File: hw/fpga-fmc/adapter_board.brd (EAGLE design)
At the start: 69 x 84 mm, 167 parts, among them IC1 M24C02, J1 5569262-1, J2 ASP-134488-01, U1 ADM3066E, U10 ADM3066E, U11 ADM3066E, U12 ADM3066E, U13 ADM3066E, U14 ADM3066E, U15 ADM3066E, U16 ADM3066E, U17 TCA9548A, U18 TXS0102, U19 TXS0102, U2 ADM3066E, U20 TXS0102, U21 TXS0102, U3 ADM3066E, U4 ADM3066E, U5 ADM3066E, U6 ADM3066E, U7 ADM3066E, U8 ADM3066E, U9 ADM3066E

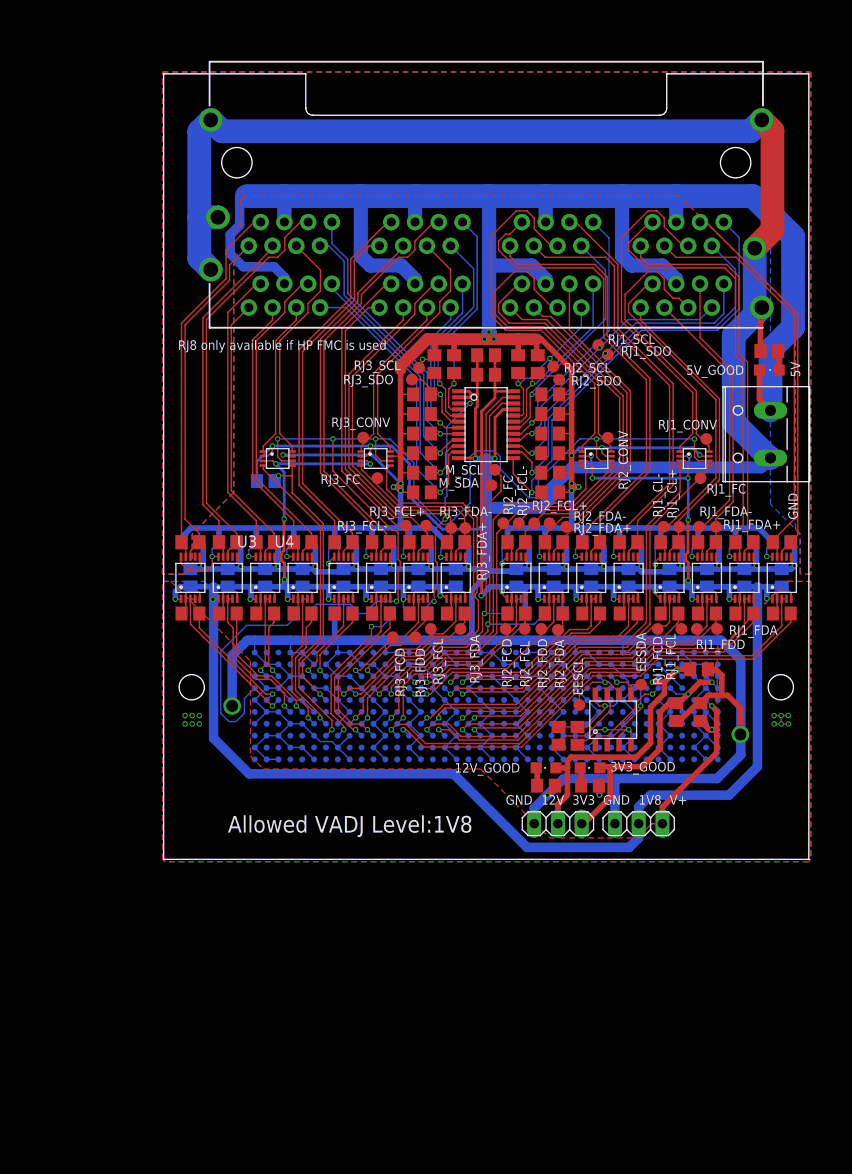
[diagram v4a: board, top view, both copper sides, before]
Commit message: hw/fpga-fmc: fix connector turned by 180 degrees. add led for 1v8. change i2c package
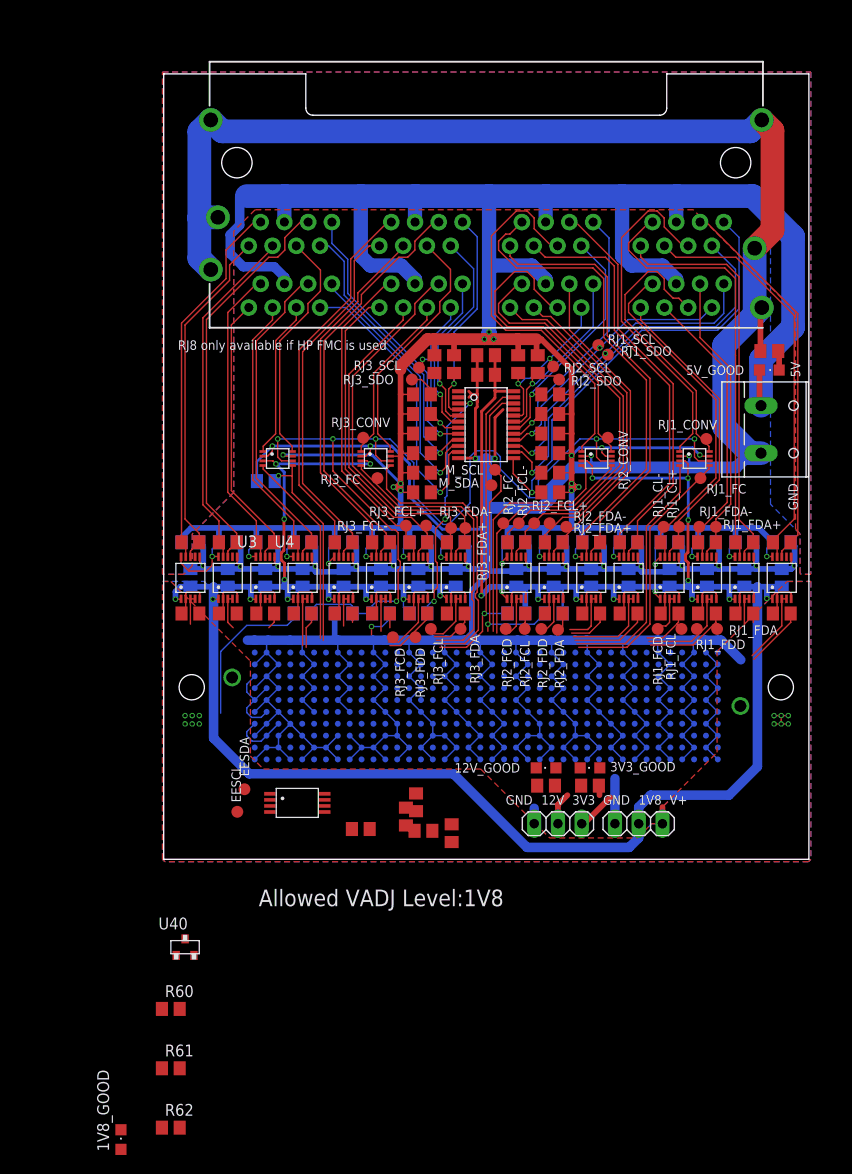
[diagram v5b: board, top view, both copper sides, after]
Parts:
- added 1V8_GOOD: (no value), led:CHIPLED_0805
- added R60: 10R, resistor:R0805
- added R61: 10k, resistor:R0805
- added R62: 130R, resistor:R0805
- added U40: IRLML2502, parts:SOT23-IRLML
- IC1: device parts:SO8N -> parts:TSSOP-8
- moved EESDA 43.9 mm to (8.64, 7.49)
- moved EESCL 38.3 mm to (7.87, 5.08)
- moved C36 36.0 mm to (21.1, 3.24), turned to 180 degrees
- moved IC1 34.9 mm to (14.3, 6.03)
- moved C37 34.2 mm to (27.8, 3.05)
- moved C35 33.4 mm to (25.9, 4.57)
- moved C39 17.0 mm to (30.8, 2.79)
- moved R52 16.8 mm to (27.0, 6.10)
- moved X1 0.57 mm to (64.5, 46.0), turned to 270 degrees
- turned J2 to 180 degrees
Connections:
- new net N$6: R60.1, R61.1, U40.P1
- new net N$8: R62.2, U40.P3
- new net N$9: 1V8_GOOD.C, R62.1
- net +3V3: now also 1V8_GOOD.A
- net 0V: now also IC1.3, IC1.4, R61.2, U40.P2, X1.2; no longer IC1.P3, IC1.P4, U17.P0, U17.P1, X1.1
- net 1V8: now also R60.2
- net 3P3VAUX: now also IC1.8; no longer IC1.P8
- net 5V: now also X1.1; no longer X1.2
- net FMC_IIC_SCL: now also IC1.6, M_SCL.TP, R6.1, U17.P21; no longer IC1.P6
- net FMC_IIC_SDA: now also IC1.5, M_SDA.TP, R5.1, U17.P22; no longer IC1.P5
- net FMC_LA05_N: no longer M_SCL.TP, R6.1, U17.P21
- net FMC_LA05_P: no longer M_SDA.TP, R5.1, U17.P22
- net GA0: now also IC1.2, U17.P1; no longer IC1.P2
- net GA1: now also IC1.1, U17.P0; no longer IC1.P1
- net N$1: now also IC1.7; no longer IC1.P7
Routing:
- net 0V: track 783.7 -> 718.4 mm, vias 38 -> 34
- net FMC_LA05_N: track 48.2 -> 0.00 mm, vias 2 -> 0
- net FMC_LA05_P: track 44.8 -> 0.00 mm, vias 2 -> 0
- net FMC_LA07_P: track 52.3 -> 7.88 mm, vias 1 -> 0
- net FMC_LA07_N: track 49.6 -> 6.52 mm, vias 1 -> 0
- net FMC_LA11_P: track 43.9 -> 3.39 mm, vias 1 -> 0
- net FMC_LA11_N: track 41.1 -> 0.95 mm, vias 1 -> 0
- net FMC_IIC_SDA: track 4.60 -> 35.4 mm
- net +12V: track 31.6 -> 3.47 mm, vias 2 -> 0
- net FMC_IIC_SCL: track 7.74 -> 33.8 mm
- net FMC_LA16_P: track 30.7 -> 5.25 mm, vias 1 -> 0
- net FMC_LA15_P: track 35.6 -> 10.9 mm, vias 1 -> 0
- net FMC_LA15_N: track 33.0 -> 9.52 mm, vias 1 -> 0
- net FMC_LA16_N: track 28.6 -> 5.72 mm, vias 1 -> 0
- net FMC_LA12_P: track 46.9 -> 26.6 mm, vias 1 -> 0
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
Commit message: hdl: copy all pin assignments to constraint file
note: RJ8 FMC connection are not connected on the FPGA board, so RJ8 cannot be used with the prototype pcb
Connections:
- net FMC_HA00_CC_N: no longer J2.F5
- net FMC_HA00_CC_P: no longer J2.F4
- net FMC_HA01_CC_N: no longer J2.E3
- net FMC_HA01_CC_P: no longer J2.E2
- net FMC_HA05_N: no longer J2.E7
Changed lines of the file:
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@@
 </signal>
 <signal name="FMC_HA01_CC_P">
-<contactref element="J2" pad="E2"/>
 <contactref element="R2" pad="2"/>
 <wire x1="3.8075" y1="26.289" x2="4.318" y2="26.289" width="0.1524" layer="1"/>
-<wire x1="4.318" y1="26.289" x2="57.995" y2="15.765" width="0" layer="19" extent="1-16"/>
 </signal>
 <signal name="FMC_HA01_CC_N">
-<contactref element="J2" pad="E3"/>
 <contactref element="U1" pad="P2"/>
 <contactref element="U1" pad="P3"/>
 <wire x1="2.8575" y1="27.849" x2="3.3575" y2="27.849" width="0.1524" layer="1"/>
 <wire x1="2.8575" y1="27.849" x2="2.8575" y2="25.146" width="0.1524" layer="1"/>
-<wire x1="2.8575" y1="25.146" x2="56.725" y2="15.765" width="0" layer="19" extent="1-16"/>
 </signal>
 <signal name="FMC_HA00_CC_P">
-<contactref element="J2" pad="F4"/>
 <contactref element="U2" pad="P2"/>
 <contactref element="U2" pad="P3"/>
@@
 <wire x1="6.858" y1="25.3365" x2="6.858" y2="27.849" width="0.1524" layer="1"/>
 <wire x1="7.4295" y1="24.765" x2="6.858" y2="25.3365" width="0.1524" layer="1"/>
-<wire x1="7.4295" y1="24.765" x2="55.455" y2="17.035" width="0" layer="19" extent="1-16"/>
 </signal>
 <signal name="FMC_HA00_CC_N">
-<contactref element="J2" pad="F5"/>
 <contactref element="R23" pad="2"/>
-<wire x1="7.808" y1="26.289" x2="54.185" y2="17.035" width="0" layer="19" extent="1-16"/>
 </signal>
 <signal name="N$2" class="3">
@@
 </signal>
 <signal name="FMC_HA05_N">
-<contactref element="J2" pad="E7"/>
 <contactref element="U18" pad="5"/>
 <contactref element="R59" pad="1"/>
@@
 <via x="12.2881" y="41.021" extent="1-16" drill="0.35"/>
 <wire x1="12.2881" y1="41.021" x2="13.742" y2="41.021" width="0.1524" layer="1"/>
-<wire x1="17.0688" y1="23.4188" x2="51.645" y2="15.765" width="0" layer="19" extent="1-16"/>
 </signal>
 <signal name="N$6">

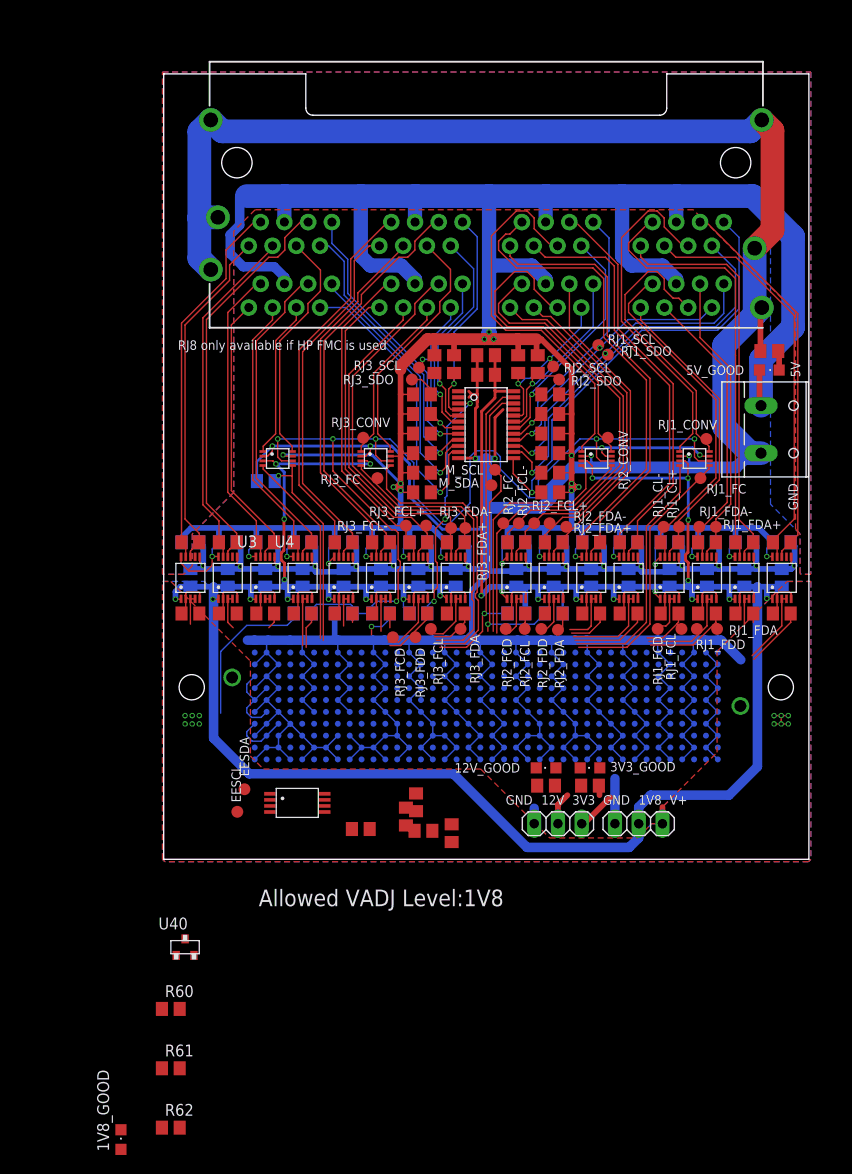
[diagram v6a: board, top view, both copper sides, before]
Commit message: turn FMC connector and reroute signals
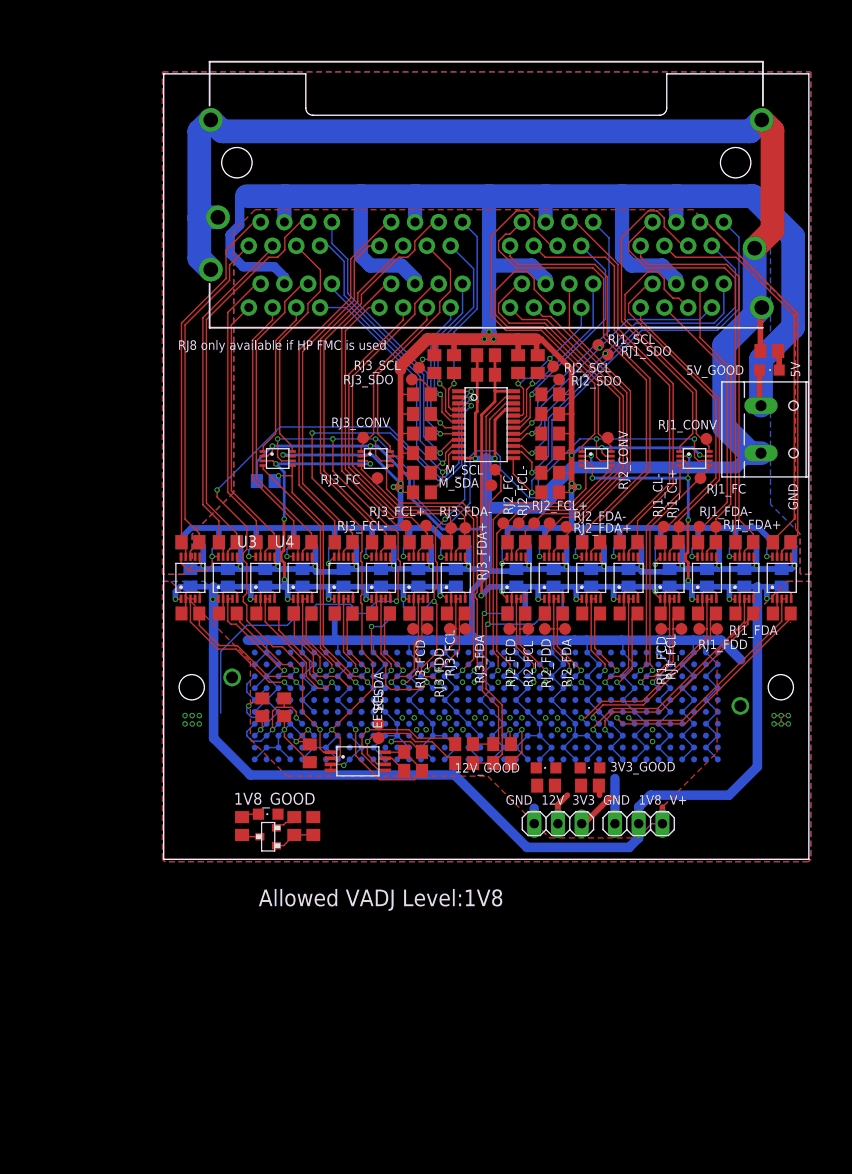
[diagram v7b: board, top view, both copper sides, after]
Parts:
- added R63, R64: 0R, rcl:R0805
- added R65, R66: 0R DNP, rcl:R0805
- R57: value 0R -> 0R DNP
- R59: value NB -> DNP
- moved 1V8_GOOD 38.2 mm to (11.2, 4.83), turned to 90 degrees
- moved R62 33.1 mm to (8.38, 3.56), turned to 270 degrees
- moved R61 29.1 mm to (14.0, 3.56), turned to 90 degrees
- moved R60 24.8 mm to (16.0, 3.56), turned to 90 degrees
- moved C35 19.3 mm to (10.5, 16.3), turned to 90 degrees
- moved EESCL 17.0 mm to (23.0, 13.0)
- moved EESDA 16.0 mm to (23.0, 14.5)
- moved C36 15.4 mm to (12.9, 16.3), turned to 90 degrees
- moved U40 14.8 mm to (11.2, 2.41), turned to 90 degrees
- moved C37 14.7 mm to (15.6, 11.3), turned to 90 degrees
- moved C39 9.63 mm to (26.7, 11.5), turned to 180 degrees
- moved IC1 7.86 mm to (20.8, 10.5)
- moved R52 3.38 mm to (26.7, 9.46), turned to 0 degrees
- moved RJ3_FCD 2.33 mm to (26.7, 24.6)
- moved RJ3_FDD 2.03 mm to (30.6, 24.6)
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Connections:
- removed net FMC_HA00_CC_N: R23.2
- removed net FMC_HA00_CC_P: U2.P2, U2.P3
- removed net FMC_HA01_CC_N: U1.P2, U1.P3
- removed net FMC_HA01_CC_P: R2.2
- removed net FMC_HA05_N: R59.1, U18.5
- removed net I2C_RESET: R7.1, U17.P2
- new net FMC_LA17_CC_N: J2.D21
- new net FMC_LA17_CC_P: J2.D20
- new net FMC_LA18_CC_N: J2.C23
- new net FMC_LA18_CC_P: J2.C22
- new net FMC_LA19_N: J2.H23, RJ3_FC.TP, U19.4
- new net FMC_LA19_P: J2.H22, U19.5
- new net FMC_LA20_N: J2.G22
- new net FMC_LA20_P: J2.G21
- new net FMC_LA21_N: J2.H26, RJ3_FDD.TP, U8.P2, U8.P3
- new net FMC_LA21_P: J2.H25, R35.2, RJ3_FDA.TP
- new net FMC_LA22_N: J2.G25, R57.2
- new net FMC_LA22_P: J2.G24, R7.1, U17.P2
- new net FMC_LA23_N: J2.D24
- new net FMC_LA23_P: J2.D23
- new net FMC_LA24_N: J2.H29, U6.P2, U6.P3
- new net FMC_LA24_P: J2.H28, R31.2
- new net FMC_LA25_N: J2.G28, RJ3_FCD.TP, U7.P2, U7.P3
- new net FMC_LA25_P: J2.G27, R33.2, RJ3_FCL.TP
- new net FMC_LA26_N: J2.D27
- new net FMC_LA26_P: J2.D26
- new net FMC_LA27_N: J2.C27
- new net FMC_LA27_P: J2.C26
- new net FMC_LA28_N: J2.H32, U5.P2, U5.P3
- new net FMC_LA28_P: J2.H31, R29.2
- new net FMC_LA29_N: J2.G31, U18.4
- new net FMC_LA29_P: J2.G30, R59.1, U18.5
- new net FMC_LA30_N: J2.H35, U4.P2, U4.P3
- new net FMC_LA30_P: J2.H34, R27.2
- new net FMC_LA31_N: J2.G34, R25.2
- new net FMC_LA31_P: J2.G33, U3.P2, U3.P3
- new net FMC_LA32_N: J2.H38, U2.P2, U2.P3
- new net FMC_LA32_P: J2.H37, R23.2
- new net FMC_LA33_N: J2.G37, U1.P2, U1.P3
- new net FMC_LA33_P: J2.G36, R2.2
- new net I2C_SCL: M_SCL.TP, R6.1, R64.2, R66.1, U17.P21
- new net I2C_SDA: M_SDA.TP, R5.1, R63.2, R65.1, U17.P22
- net FMC_DP0_C2M_N: no longer R25.2
- net FMC_DP0_C2M_P: no longer U3.P2, U3.P3
- net FMC_DP0_M2C_N: no longer R29.2
- net FMC_DP0_M2C_P: no longer U5.P2, U5.P3
- net FMC_IIC_SCL: now also R64.1; no longer M_SCL.TP, R6.1, U17.P21
- net FMC_IIC_SDA: now also R63.1; no longer M_SDA.TP, R5.1, U17.P22
- net FMC_LA00_CC_N: now also RJ1_FCD.TP, U13.P2, U13.P3; no longer R27.2
- net FMC_LA00_CC_P: now also R45.2, RJ1_FCL.TP; no longer U4.P2, U4.P3
- net FMC_LA01_CC_N: now also R51.2; no longer R35.2, RJ3_FDA.TP
- net FMC_LA01_CC_P: now also U16.P2, U16.P3; no longer RJ3_FDD.TP, U8.P2, U8.P3
- net FMC_LA02_N: now also U21.4; no longer R57.2
- net FMC_LA02_P: now also RJ1_FC.TP, U21.5; no longer U18.4
- net FMC_LA03_N: now also U12.P2, U12.P3; no longer U19.5
- net FMC_LA03_P: now also R43.2; no longer RJ3_FC.TP, U19.4
- net FMC_LA04_N: now also U11.P2, U11.P3; no longer R31.2
- net FMC_LA04_P: now also R41.2; no longer U6.P2, U6.P3
- net FMC_LA05_N: now also RJ1_FDD.TP, U14.P2, U14.P3
- net FMC_LA05_P: now also R47.2, RJ1_FDA.TP
- net FMC_LA06_N: now also U15.P2, U15.P3; no longer R33.2, RJ3_FCL.TP
- net FMC_LA06_P: now also R49.2; no longer RJ3_FCD.TP, U7.P2, U7.P3
- net FMC_LA07_N: now also RJ2_FDD.TP, U10.P2, U10.P3; no longer R51.2
- net FMC_LA07_P: now also R39.2, RJ2_FDA.TP; no longer U16.P2, U16.P3
- net FMC_LA08_N: no longer RJ2_FC.TP, U20.5
- net FMC_LA08_P: no longer U20.4
- net FMC_LA09_N: no longer R39.2, RJ2_FDA.TP
- net FMC_LA09_P: no longer RJ2_FDD.TP, U10.P2, U10.P3
- net FMC_LA10_N: no longer R37.2, RJ2_FCL.TP
- net FMC_LA10_P: no longer RJ2_FCD.TP, U9.P2, U9.P3
- net FMC_LA11_N: now also RJ2_FCD.TP, U9.P2, U9.P3; no longer R49.2
- net FMC_LA11_P: now also R37.2, RJ2_FCL.TP; no longer U15.P2, U15.P3
- net FMC_LA12_N: no longer RJ1_FC.TP, U21.5
- net FMC_LA12_P: no longer U21.4
- net FMC_LA13_N: no longer R43.2
- net FMC_LA13_P: no longer U12.P2, U12.P3
- net FMC_LA14_N: now also R65.2; no longer R41.2
- net FMC_LA14_P: now also R66.2; no longer U11.P2, U11.P3
- net FMC_LA15_N: now also U20.4; no longer R47.2, RJ1_FDA.TP
- net FMC_LA15_P: now also RJ2_FC.TP, U20.5; no longer RJ1_FDD.TP, U14.P2, U14.P3
- net FMC_LA16_N: no longer R45.2, RJ1_FCL.TP
- net FMC_LA16_P: no longer RJ1_FCD.TP, U13.P2, U13.P3
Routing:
- net GA1: track 0.00 -> 76.7 mm, vias 0 -> 3
- net GA0: track 0.00 -> 69.3 mm, vias 0 -> 3
- net I2C_SCL: track 0.00 -> 51.0 mm, vias 0 -> 1
- net I2C_SDA: track 0.00 -> 45.1 mm, vias 0 -> 1
- net FMC_LA22_P: track 0.00 -> 37.5 mm, vias 0 -> 4
- net FMC_LA19_N: track 0.00 -> 32.9 mm, vias 0 -> 1
- net FMC_LA19_P: track 0.00 -> 31.2 mm, vias 0 -> 1
- net FMC_LA29_P: track 0.00 -> 30.1 mm, vias 0 -> 2
- net FMC_LA12_N: track 28.3 -> 0.00 mm
- net FMC_LA29_N: track 0.00 -> 28.2 mm, vias 0 -> 1
- net FMC_LA12_P: track 26.6 -> 0.00 mm
- net I2C_RESET: track 25.8 -> 0.00 mm, vias 3 -> 0
- net FMC_LA08_N: track 26.4 -> 0.90 mm, vias 0 -> 1
- net FMC_LA08_P: track 25.9 -> 0.90 mm, vias 0 -> 1
- net FMC_LA05_N: track 0.00 -> 23.9 mm, vias 0 -> 1
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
